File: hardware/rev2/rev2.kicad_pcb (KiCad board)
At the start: 4 copper layers, 60 x 40 mm, 101 parts, among them J1 USB_C_Receptacle_USB2.0_16P, J2 SMA, J3 SMA, J6 SMA, J7 SMA, SW1 SW_Push, SW2 SW_Push, U1 EClamp2522P, U2 ESP32-S3FN8, U3 SX1262IMLTRT, U4 PE4259, Y1 ECS-2520SMV-400-FN-TR, Y2 TXO-20CSMV-320

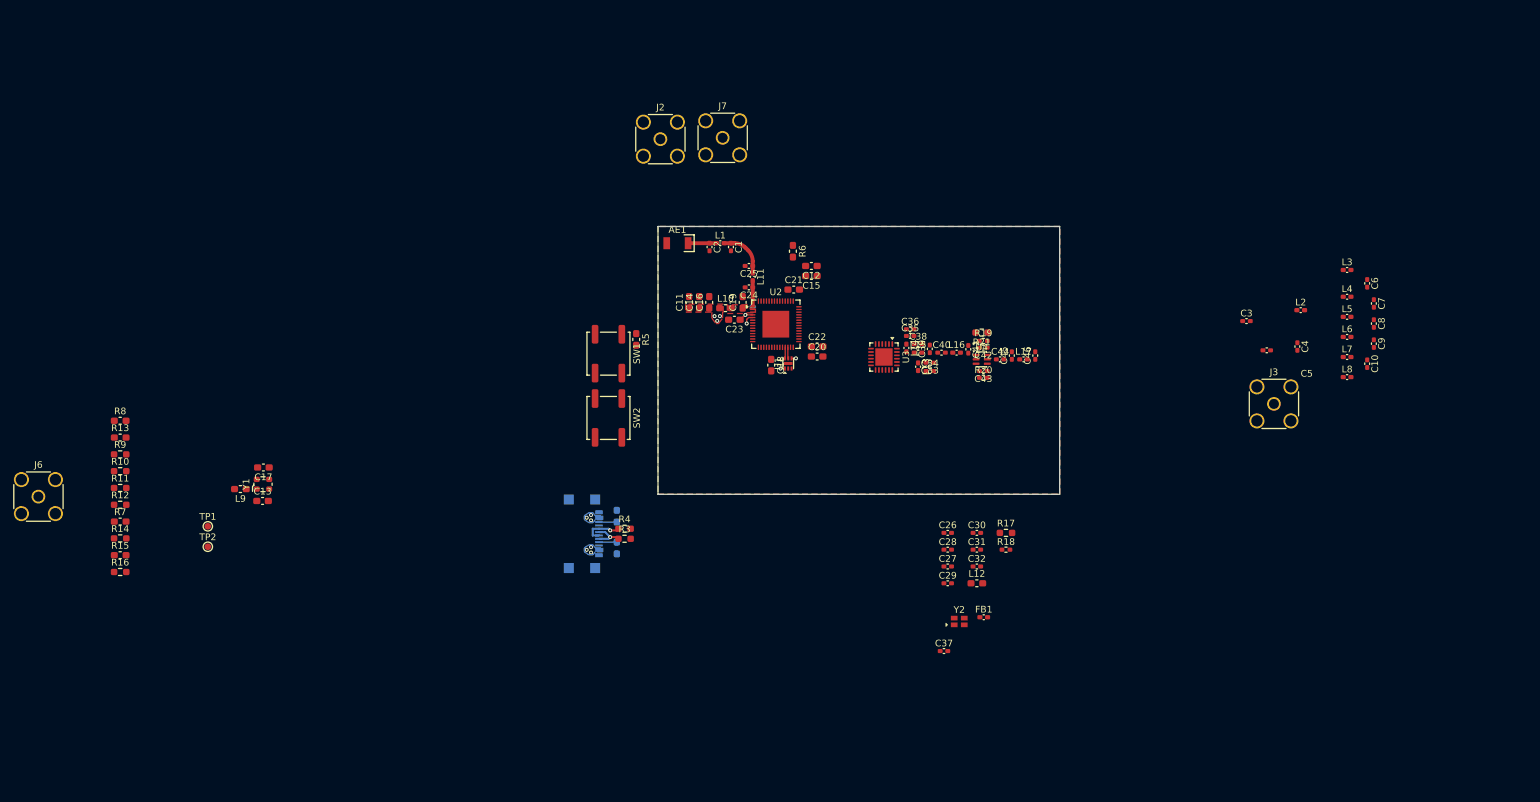
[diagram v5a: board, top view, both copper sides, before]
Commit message: continued layout, finished most of the RF stuff
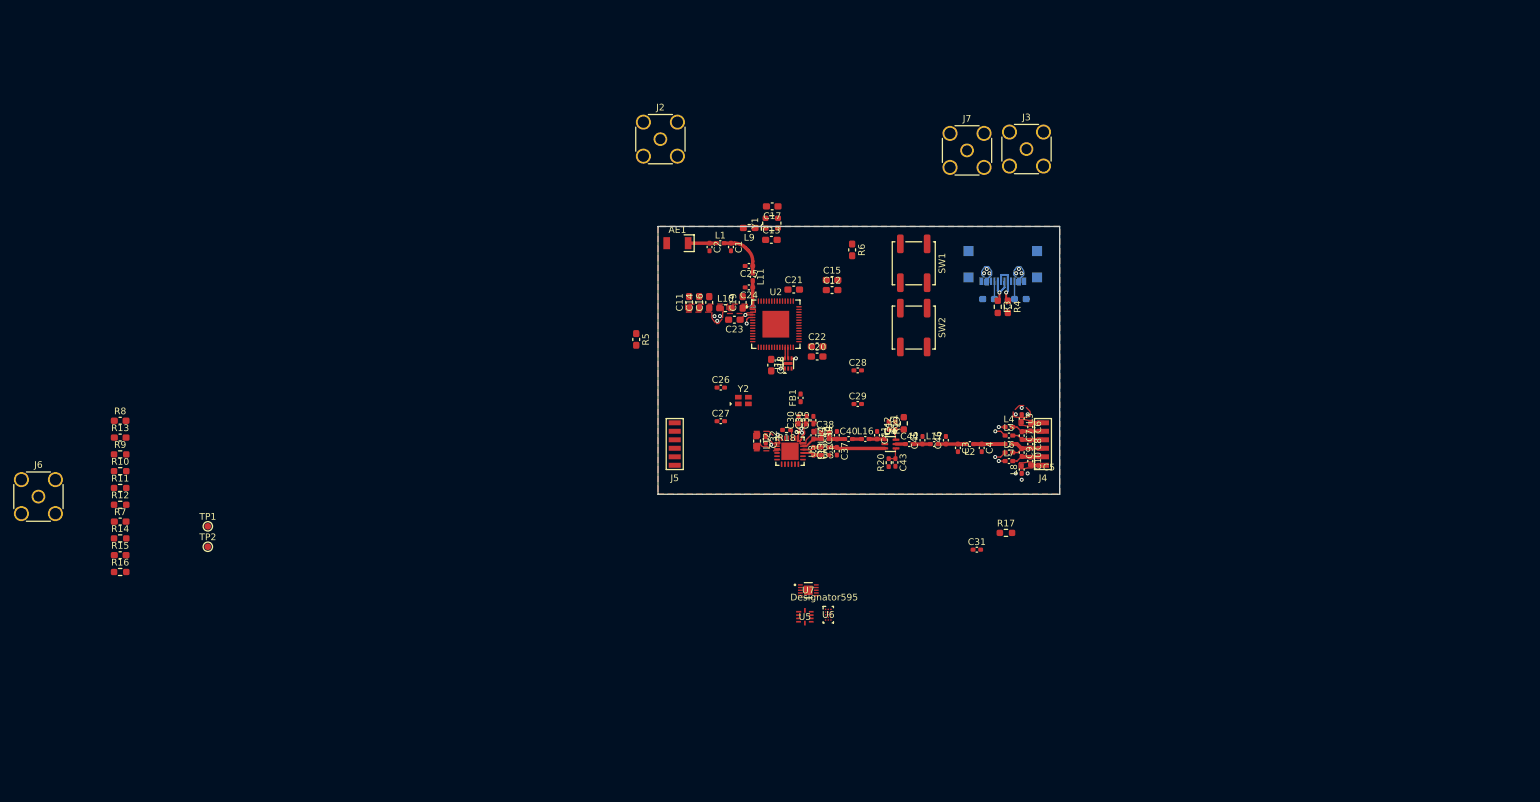
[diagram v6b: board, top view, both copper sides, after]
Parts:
- added J4: Antenna RF and GNSS Data, _footprints:Antenna_Conn, F.Cu at (185.5, 89.5)
- added J5: Antenna GND, _footprints:Antenna_Conn, F.Cu at (130.5, 89.5)
- added U5: MP2664GG-xxxx-P, _footprints:QFN-2x2_MP2664_MNP, F.Cu at (149.9, 115.3)
- added U6: TPS63805YFFR, _footprints:YFF0015AHAN, F.Cu at (153.4, 115.0)
- added U7: MAX17055ETB+, _footprints:21-100013A_T102A2+1C_MXM, F.Cu at (150.5, 111.3)
- moved C13 85.4 mm to (144.9, 59.0)
- moved C17 85.4 mm to (145.1, 54.0)
- moved L9 85.4 mm to (141.6, 57.2)
- moved Y1 85.4 mm to (145.0, 56.5)
- moved J1 76.2 mm to (179.5, 61.5), turned to 0 degrees
- moved R2 68.4 mm to (182.1, 67.8), turned to 0 degrees
- moved R1 66.8 mm to (177.4, 67.8), turned to 180 degrees
- moved R4 66.2 mm to (180.2, 69.0), turned to -90 degrees
- moved R3 65.6 mm to (178.8, 69.0), turned to -90 degrees
- moved C7 56.2 mm to (182.3, 88.2)
- moved C9 55.1 mm to (182.3, 90.8)
- moved C6 54.7 mm to (183.6, 87.0)
- moved C8 54.4 mm to (183.6, 89.5)
- moved L4 54.1 mm to (180.4, 87.0)
- moved L5 53.5 mm to (180.4, 88.2)
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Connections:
- net Net-(U3-VR_PA) renamed /SX1262/VR_PA
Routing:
- net Net-(U4-RF2): track 0.00 -> 8.41 mm
- net Net-(J4-Pin_4): track 0.00 -> 6.40 mm
- net Net-(J4-Pin_5): track 0.00 -> 4.83 mm
- net Net-(J4-Pin_2): track 0.00 -> 4.83 mm
- net Net-(J4-Pin_3): track 0.00 -> 4.77 mm
- net Net-(J3-In): track 0.00 -> 4.70 mm
- net Net-(U3-RFO): track 0.00 -> 4.19 mm
- net /Antenna_LoRa: track 0.00 -> 4.18 mm
- net Net-(U4-~{CTRL}): track 0.00 -> 3.82 mm
- net Net-(C38-Pad2): track 0.00 -> 3.37 mm
- net Net-(U3-RFI_P): track 0.00 -> 2.88 mm
- net Net-(U3-RFI_N): track 0.00 -> 2.88 mm
- net Net-(C44-Pad2): track 0.00 -> 2.58 mm
- net Net-(U4-CTRL): track 0.00 -> 2.57 mm
- net Net-(U4-RF1): track 0.00 -> 2.38 mm
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- added copper zone on F.Cu, net /SX1262/VR_PA
- added copper zone on F.Cu, net Net-(J4-Pin_1)
- added copper zone on F.Cu, net Net-(J4-Pin_6)
- added copper zone on F.Cu, net Net-(U3-DCC_SW)
- added copper zone on F.Cu, net Net-(U3-VREG)

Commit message: modified layout
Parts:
- moved C20 42.2 mm to (112.7, 92.3)
- moved C21 42.2 mm to (109.2, 82.3)
- moved C22 42.2 mm to (112.7, 90.8)
- moved C12 42.2 mm to (115.0, 82.4)
- moved C15 42.2 mm to (115.0, 80.9)
- moved R6 42.2 mm to (118.0, 76.4)
- moved SW1 31.3 mm to (197.0, 57.1)
- moved SW2 31.3 mm to (197.0, 66.7)
- moved J1 30.3 mm to (209.5, 57.0)
- moved R1 30.3 mm to (207.4, 63.3)
- moved R2 30.3 mm to (212.1, 63.3)
- moved R3 30.3 mm to (208.8, 64.5)
- moved R4 30.3 mm to (210.2, 64.5)
- moved R5 18.2 mm to (107.0, 77.8)
- moved C11 8.25 mm to (138.1, 74.5), turned to 180 degrees
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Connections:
- net /D+* renamed /*D+
- net /D-* renamed /*D-
- U6 pad E2: +3.3V -> +3V3
- U6 pad E3: +3.3V -> +3V3
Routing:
- net /Antenna_WiFi: track 7.49 -> 2.08 mm
- net /ESP32/LNA_IN: track 3.74 -> 2.45 mm
- removed copper zone on B.Cu, net /ESP32/LNA_IN
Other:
- board text added: "MOVE TO MIDDLE"

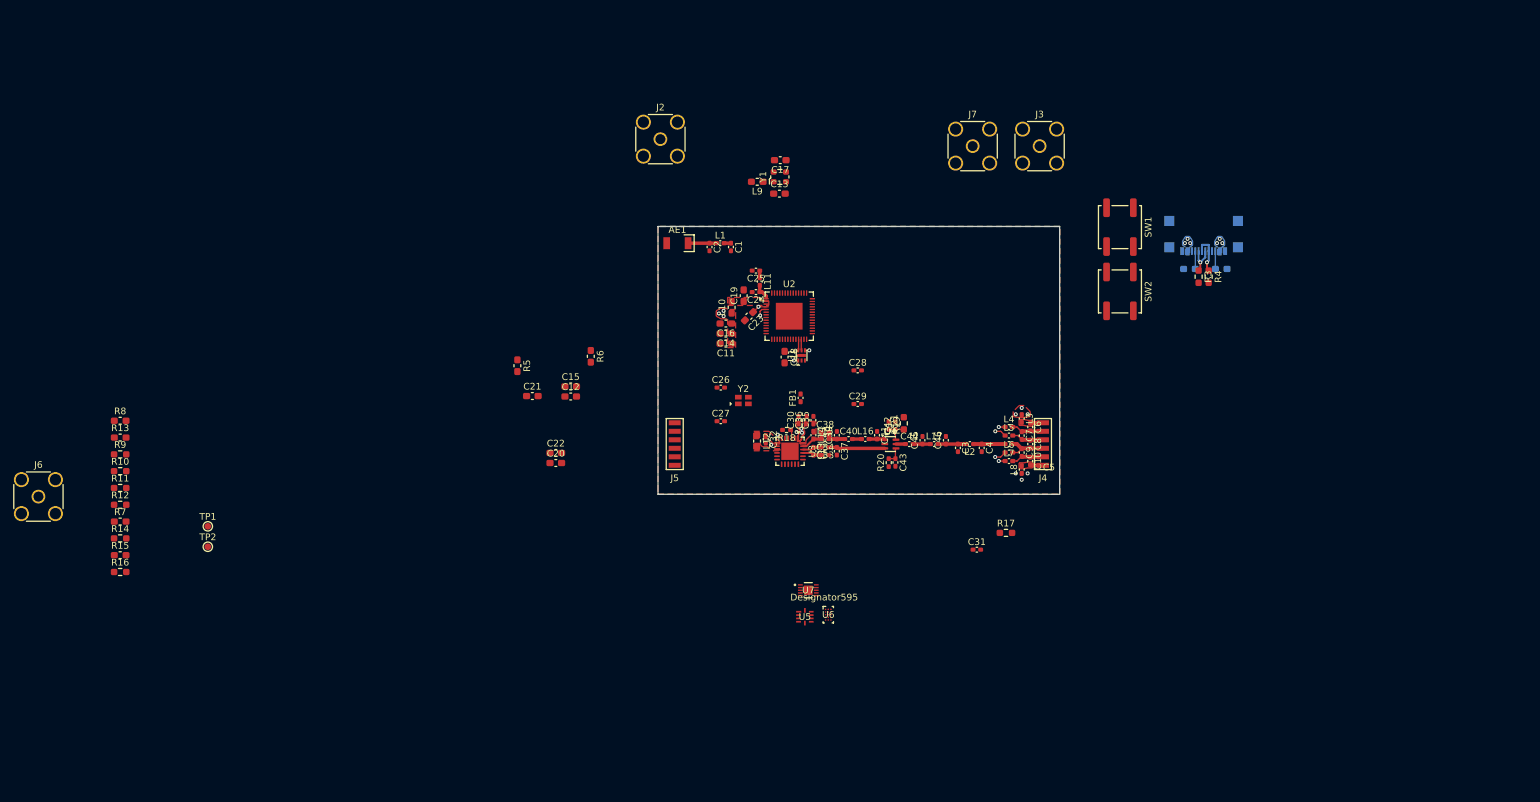
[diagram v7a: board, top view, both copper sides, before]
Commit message: finished routing most of the RF and power for SX1262 and ESP32, also decided final ish positions for both.
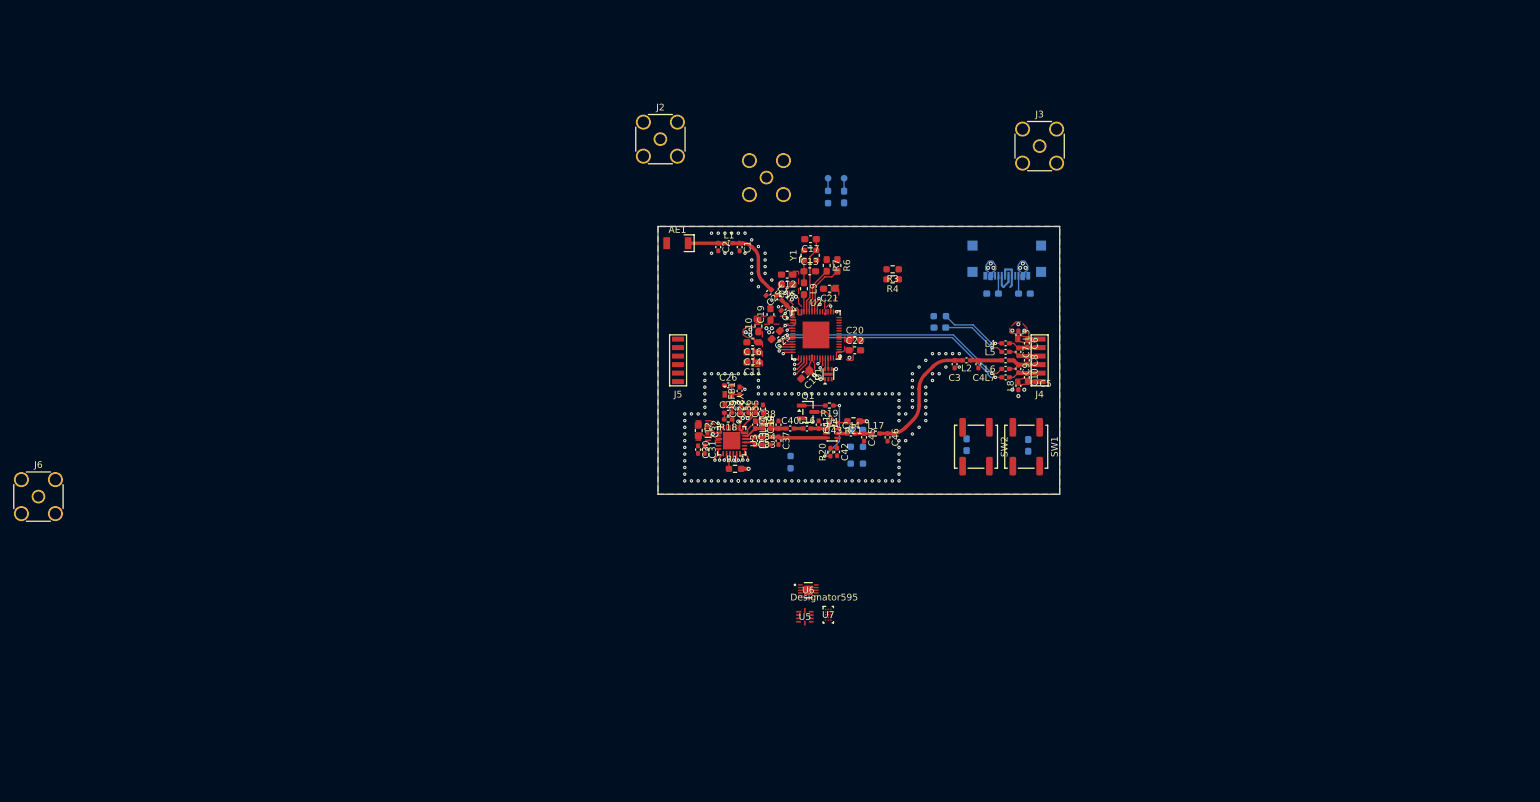
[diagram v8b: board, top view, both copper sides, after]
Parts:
- added Q1: SS8050, Package_TO_SOT_SMD:SOT-23, F.Cu at (150.4, 84.7)
- J2, J3: value SMA -> uFL
- J7, R10, R11, R12, R13, R14, R15, R16, R5, R8, R9, TP1, TP2: moved to B.Cu
- moved R16 128.3 mm to (170.1, 70.4)
- moved R15 127.1 mm to (170.1, 72.1)
- moved R8 126.5 mm to (174.1, 89.6), turned to 90 degrees
- moved R14 117.4 mm to (153.4, 52.6), turned to 90 degrees
- moved R13 113.9 mm to (155.8, 52.6), turned to 90 degrees
- moved R7 112.2 mm to (153.2, 62.8), turned to -90 degrees
- moved R12 110.6 mm to (157.7, 87.4)
- moved R11 110.2 mm to (157.7, 89.9)
- moved R10 110.0 mm to (157.7, 92.4)
- moved TP1 108.3 mm to (155.8, 49.8)
- moved TP2 107.8 mm to (153.4, 49.8)
- moved R9 100.1 mm to (147.8, 92.2), turned to 90 degrees
- moved R5 77.2 mm to (183.3, 89.7), turned to 90 degrees
- moved C20 48.3 mm to (157.4, 74.0)
- moved C22 47.2 mm to (157.4, 75.5)
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- renumbered C43 to C42, C42 to C43, U7 to U6, U6 to U7
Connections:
- C43 pad 1: Net-(U4-~{CTRL}) -> Net-(Q1-C)
- FB1 pad 1: /SX1262/DIO3 -> Net-(Y2-VDD)
- FB1 pad 2: Net-(Y2-VDD) -> /SX1262/DIO3
- R19 pad 1: /ESP32/RX_EN -> /SX1262/DIO2
- R19 pad 2: Net-(U4-~{CTRL}) -> Net-(Q1-B)
- R21 pad 1: Net-(U4-~{CTRL}) -> +3V3
- R21 pad 2: +3V3 -> Net-(Q1-C)
- U2 pad 43: unconnected-(U2-GPIO38-Pad43) -> /Power/INT
- U2 pad 44: unconnected-(U2-MTCK-Pad44) -> /ESP32/ALRT
- U4 pad 6: Net-(U4-~{CTRL}) -> Net-(Q1-C)
- U6 pad 8: /Power/ALRT -> /ESP32/ALRT
- Y2 pad 2: (no net) -> GND
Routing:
- net /EXTINT: track 0.95 -> 37.1 mm, vias 1 -> 2
- net /RESET_N: track 1.76 -> 35.9 mm, vias 1 -> 2
- net /Antenna_LoRa: track 4.18 -> 19.3 mm
- net /SX1262/DIO2: track 0.00 -> 12.1 mm, vias 0 -> 3
- net Net-(U2-XTAL_N): track 0.00 -> 11.5 mm
- net /RXD/SDA: track 0.95 -> 10.0 mm
- net /Antenna_WiFi: track 2.08 -> 10.5 mm
- net /ESP32/GPIO45: track 0.00 -> 8.23 mm
- net /TXD/SCL: track 1.76 -> 9.92 mm
- net /ESP32/GPIO46: track 0.00 -> 7.13 mm
- net Net-(Q1-C): track 0.00 -> 6.83 mm
- net /SX1262/Reset: track 0.00 -> 4.58 mm, vias 0 -> 2
- net +5V: track 4.63 -> 0.63 mm
- net Net-(U4-~{CTRL}): track 3.82 -> 0.00 mm
- net Net-(Q1-B): track 0.00 -> 3.54 mm
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- removed copper zone on In2.Cu, net +5V
